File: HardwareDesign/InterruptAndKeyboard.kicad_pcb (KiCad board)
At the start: 2 copper layers, 150 x 90 mm, 39 parts, among them J001 Conn_02x40_Odd_Even, J501 Conn_01x20, J503 Conn_01x02, U401 74HCT74, U402 74HCT11, U403 74HCT147, U404 74HCT540, U405 74HCT574, U406 74HCT32, U407 74HCT32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

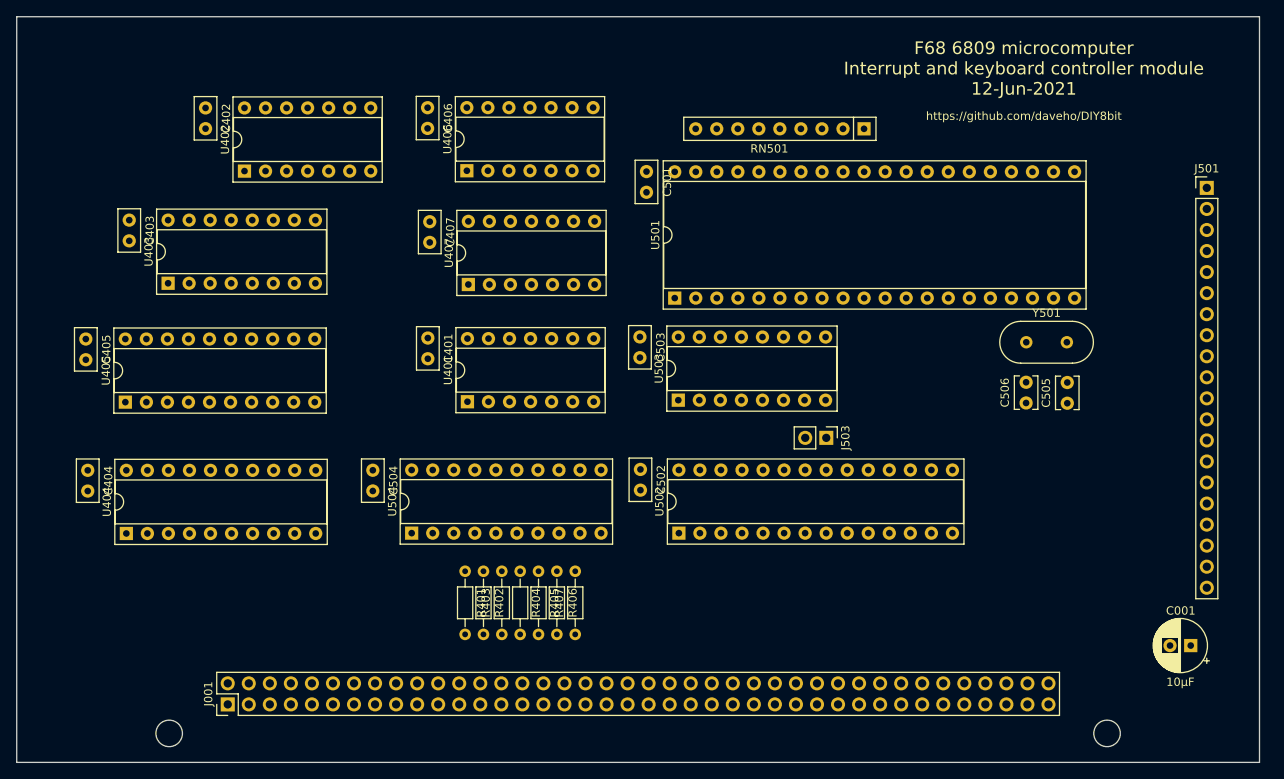
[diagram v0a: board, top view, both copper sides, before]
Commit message: tweak component placement
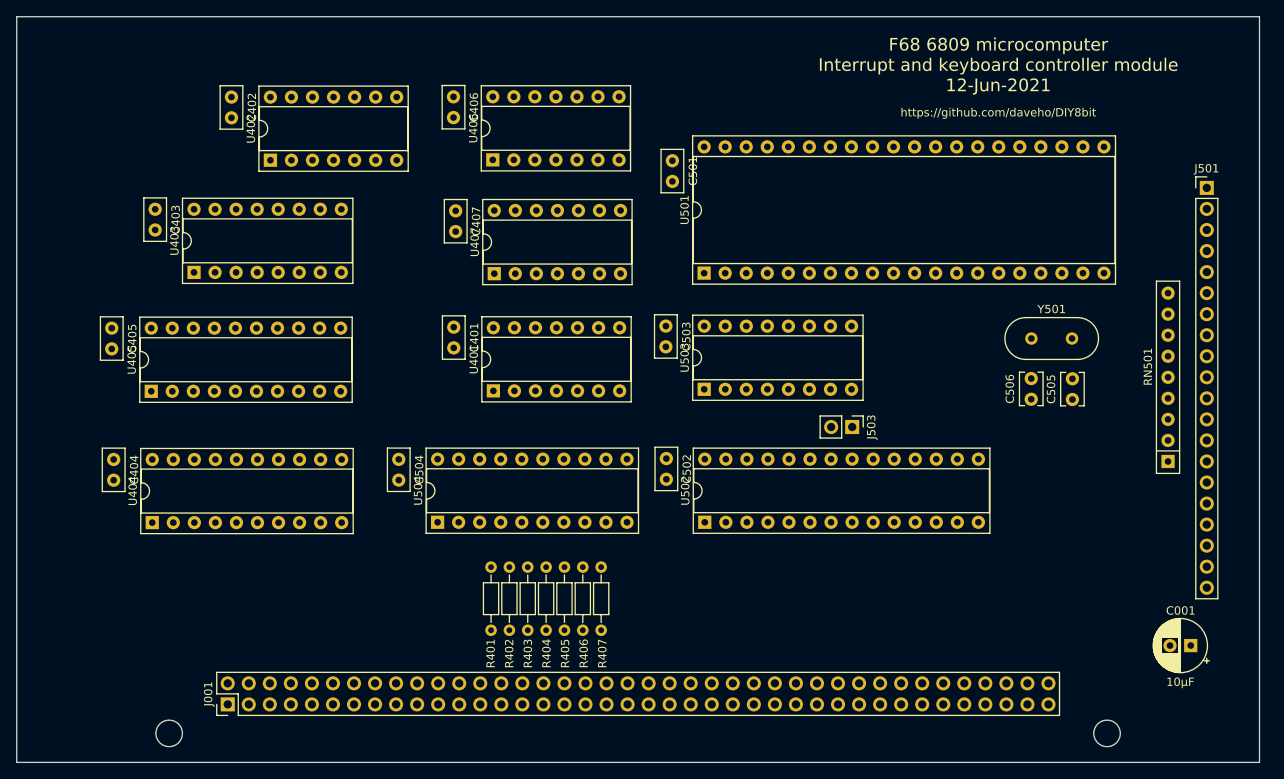
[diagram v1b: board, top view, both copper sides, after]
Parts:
- moved RN501 54.4 mm to (139.0, 53.7), turned to 90 degrees
- moved U501 4.65 mm to (83.0, 30.9)
- moved U503 3.39 mm to (83.0, 45.0)
- moved J503 3.39 mm to (100.8, 49.5)
- moved C401 3.39 mm to (52.8, 37.5)
- moved C504 3.39 mm to (46.1, 53.4)
- moved U401 3.39 mm to (57.5, 45.2)
- moved C402 3.39 mm to (25.9, 9.70)
- moved U402 3.39 mm to (30.6, 17.3)
- moved U406 3.39 mm to (57.5, 17.3)
- moved U407 3.39 mm to (57.6, 31.0)
- moved C403 3.39 mm to (16.7, 23.2)
- moved C404 3.39 mm to (11.7, 53.4)
- moved U403 3.39 mm to (21.4, 30.9)
- moved U405 3.39 mm to (16.2, 45.2)
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
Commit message: silkscreen tweaks
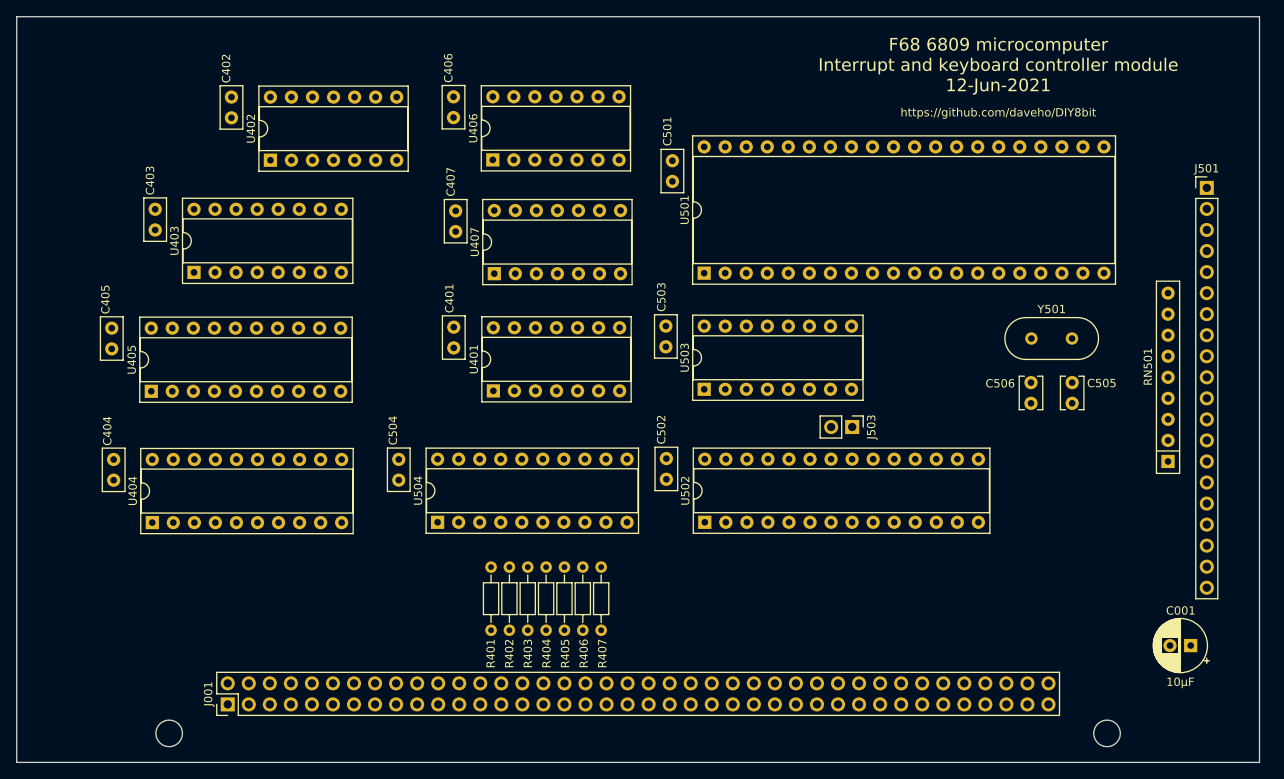
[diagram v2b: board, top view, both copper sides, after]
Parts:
- moved C506 0.49 mm to (122.4, 46.7)
- moved C505 0.46 mm to (127.4, 46.7)
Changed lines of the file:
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@@
     (descr "C, Disc series, Radial, pin pitch=2.50mm, , diameter*width=5*2.5mm^2, Capacitor, http://cdn-reichelt.de/documents/datenblatt/B300/DS_KERKO_TC.pdf")
     (tags "C Disc series Radial pin pitch 2.50mm  diameter 5mm width 2.5mm Capacitor")
-    (fp_text reference C401 (at 1.25 -2.5 90) (layer F.SilkS)
-      (effects (font (size 1 1) (thickness 0.15)))
-    )
-    (fp_text value "0.1 μF" (at 1.25 2.5 90) (layer F.Fab)
+    (fp_text reference C401 (at -3.48 0.5 90) (layer F.SilkS)
+      (effects (font (size 1 1) (thickness 0.15)))
+    )
+    (fp_text value "0.1 μF" (at -4.09 -0.8 90) (layer F.Fab)
       (effects (font (size 1 1) (thickness 0.15)))
     )
@@
     (descr "C, Disc series, Radial, pin pitch=2.50mm, , diameter*width=5*2.5mm^2, Capacitor, http://cdn-reichelt.de/documents/datenblatt/B300/DS_KERKO_TC.pdf")
     (tags "C Disc series Radial pin pitch 2.50mm  diameter 5mm width 2.5mm Capacitor")
-    (fp_text reference C402 (at 1.25 -2.5 90) (layer F.SilkS)
-      (effects (font (size 1 1) (thickness 0.15)))
-    )
-    (fp_text value "0.1 μF" (at 1.25 2.5 90) (layer F.Fab)
+    (fp_text reference C402 (at -3.46 0.62 90) (layer F.SilkS)
+      (effects (font (size 1 1) (thickness 0.15)))
+    )
+    (fp_text value "0.1 μF" (at -4.06 -0.65 90) (layer F.Fab)
       (effects (font (size 1 1) (thickness 0.15)))
     )
@@
     (descr "C, Disc series, Radial, pin pitch=2.50mm, , diameter*width=5*2.5mm^2, Capacitor, http://cdn-reichelt.de/documents/datenblatt/B300/DS_KERKO_TC.pdf")
     (tags "C Disc series Radial pin pitch 2.50mm  diameter 5mm width 2.5mm Capacitor")
-    (fp_text reference C403 (at 1.25 -2.5 90) (layer F.SilkS)
-      (effects (font (size 1 1) (thickness 0.15)))
-    )
-    (fp_text value "0.1 μF" (at 1.25 2.5 90) (layer F.Fab)
+    (fp_text reference C403 (at -3.48 0.59 90) (layer F.SilkS)
+      (effects (font (size 1 1) (thickness 0.15)))
+    )
+    (fp_text value "0.1 μF" (at -4.1 -0.66 90) (layer F.Fab)
       (effects (font (size 1 1) (thickness 0.15)))
     )
@@
     (descr "C, Disc series, Radial, pin pitch=2.50mm, , diameter*width=5*2.5mm^2, Capacitor, http://cdn-reichelt.de/documents/datenblatt/B300/DS_KERKO_TC.pdf")
     (tags "C Disc series Radial pin pitch 2.50mm  diameter 5mm width 2.5mm Capacitor")
-    (fp_text reference C404 (at 1.25 -2.5 90) (layer F.SilkS)
-      (effects (font (size 1 1) (thickness 0.15)))
-    )
-    (fp_text value "0.1 μF" (at 1.25 2.5 90) (layer F.Fab)
+    (fp_text reference C404 (at -3.44 0.74 90) (layer F.SilkS)
+      (effects (font (size 1 1) (thickness 0.15)))
+    )
+    (fp_text value "0.1 μF" (at -4.04 -0.54 90) (layer F.Fab)
       (effects (font (size 1 1) (thickness 0.15)))
     )
@@
     (descr "C, Disc series, Radial, pin pitch=2.50mm, , diameter*width=5*2.5mm^2, Capacitor, http://cdn-reichelt.de/documents/datenblatt/B300/DS_KERKO_TC.pdf")
     (tags "C Disc series Radial pin pitch 2.50mm  diameter 5mm width 2.5mm Capacitor")
-    (fp_text reference C405 (at 1.25 -2.5 90) (layer F.SilkS)
-      (effects (font (size 1 1) (thickness 0.15)))
-    )
-    (fp_text value "0.1 μF" (at 1.25 2.5 90) (layer F.Fab)
+    (fp_text reference C405 (at -3.47 0.74 90) (layer F.SilkS)
+      (effects (font (size 1 1) (thickness 0.15)))
+    )
+    (fp_text value "0.1 μF" (at -4.06 -0.62 90) (layer F.Fab)
       (effects (font (size 1 1) (thickness 0.15)))
     )
@@
     (descr "C, Disc series, Radial, pin pitch=2.50mm, , diameter*width=5*2.5mm^2, Capacitor, http://cdn-reichelt.de/documents/datenblatt/B300/DS_KERKO_TC.pdf")
     (tags "C Disc series Radial pin pitch 2.50mm  diameter 5mm width 2.5mm Capacitor")
-    (fp_text reference C406 (at 1.25 -2.5 90) (layer F.SilkS)
-      (effects (font (size 1 1) (thickness 0.15)))
-    )
-    (fp_text value "0.1 μF" (at 1.25 2.5 90) (layer F.Fab)
+    (fp_text reference C406 (at -3.48 0.6 90) (layer F.SilkS)
+      (effects (font (size 1 1) (thickness 0.15)))
+    )
+    (fp_text value "0.1 μF" (at -4.07 -0.72 90) (layer F.Fab)
       (effects (font (size 1 1) (thickness 0.15)))
     )
@@
     (descr "C, Disc series, Radial, pin pitch=2.50mm, , diameter*width=5*2.5mm^2, Capacitor, http://cdn-reichelt.de/documents/datenblatt/B300/DS_KERKO_TC.pdf")
     (tags "C Disc series Radial pin pitch 2.50mm  diameter 5mm width 2.5mm Capacitor")
-    (fp_text reference C407 (at 1.25 -2.5 90) (layer F.SilkS)
-      (effects (font (size 1 1) (thickness 0.15)))
-    )
-    (fp_text value "0.1 μF" (at 1.25 2.5 90) (layer F.Fab)
+    (fp_text reference C407 (at -3.51 0.58 90) (layer F.SilkS)
+      (effects (font (size 1 1) (thickness 0.15)))
+    )
+    (fp_text value "0.1 μF" (at -4.05 -0.62 90) (layer F.Fab)
       (effects (font (size 1 1) (thickness 0.15)))
     )
@@
     (descr "C, Disc series, Radial, pin pitch=2.50mm, , diameter*width=5*2.5mm^2, Capacitor, http://cdn-reichelt.de/documents/datenblatt/B300/DS_KERKO_TC.pdf")
     (tags "C Disc series Radial pin pitch 2.50mm  diameter 5mm width 2.5mm Capacitor")
-    (fp_text reference C501 (at 1.25 -2.5 90) (layer F.SilkS)
-      (effects (font (size 1 1) (thickness 0.15)))
-    )
-    (fp_text value "0.1 μF" (at 1.25 2.5 90) (layer F.Fab)
+    (fp_text reference C501 (at -3.55 0.59 90) (layer F.SilkS)
+      (effects (font (size 1 1) (thickness 0.15)))
+    )
+    (fp_text value "0.1 μF" (at -4.15 -0.73 90) (layer F.Fab)
       (effects (font (size 1 1) (thickness 0.15)))
     )
@@
     (descr "C, Disc series, Radial, pin pitch=2.50mm, , diameter*width=5*2.5mm^2, Capacitor, http://cdn-reichelt.de/documents/datenblatt/B300/DS_KERKO_TC.pdf")
     (tags "C Disc series Radial pin pitch 2.50mm  diameter 5mm width 2.5mm Capacitor")
-    (fp_text reference C502 (at 1.25 -2.5 90) (layer F.SilkS)
-      (effects (font (size 1 1) (thickness 0.15)))
-    )
-    (fp_text value "0.1 μF" (at 1.25 2.5 90) (layer F.Fab)
+    (fp_text reference C502 (at -3.5 0.59 90) (layer F.SilkS)
+      (effects (font (size 1 1) (thickness 0.15)))
+    )
+    (fp_text value "0.1 μF" (at -4.11 -0.68 90) (layer F.Fab)
       (effects (font (size 1 1) (thickness 0.15)))
     )
@@
     (descr "C, Disc series, Radial, pin pitch=2.50mm, , diameter*width=5*2.5mm^2, Capacitor, http://cdn-reichelt.de/documents/datenblatt/B300/DS_KERKO_TC.pdf")
     (tags "C Disc series Radial pin pitch 2.50mm  diameter 5mm width 2.5mm Capacitor")
-    (fp_text reference C503 (at 1.25 -2.5 90) (layer F.SilkS)
-      (effects (font (size 1 1) (thickness 0.15)))
-    )
-    (fp_text value "0.1 μF" (at 1.25 2.5 90) (layer F.Fab)
+    (fp_text reference C503 (at -3.51 0.52 90) (layer F.SilkS)
+      (effects (font (size 1 1) (thickness 0.15)))
+    )
+    (fp_text value "0.1 μF" (at -4.13 -0.83 90) (layer F.Fab)
       (effects (font (size 1 1) (thickness 0.15)))
     )
@@
     (descr "C, Disc series, Radial, pin pitch=2.50mm, , diameter*width=5*2.5mm^2, Capacitor, http://cdn-reichelt.de/documents/datenblatt/B300/DS_KERKO_TC.pdf")
     (tags "C Disc series Radial pin pitch 2.50mm  diameter 5mm width 2.5mm Capacitor")
-    (fp_text reference C504 (at 1.25 -2.5 90) (layer F.SilkS)
-      (effects (font (size 1 1) (thickness 0.15)))
-    )
-    (fp_text value "0.1 μF" (at 1.25 2.5 90) (layer F.Fab)
+    (fp_text reference C504 (at -3.49 0.68 90) (layer F.SilkS)
+      (effects (font (size 1 1) (thickness 0.15)))
+    )
+    (fp_text value "0.1 μF" (at -4.08 -0.61 90) (layer F.Fab)
       (effects (font (size 1 1) (thickness 0.15)))
     )
@@
   )
   (module Capacitor_THT:C_Disc_D3.8mm_W2.6mm_P2.50mm (layer Front)
-    (at 127.42 46.2 90)
+    (at 127.39 46.66 90)
     (descr "C, Disc series, Radial, pin pitch=2.50mm, , diameter*width=3.8*2.6mm^2, Capacitor, http://www.vishay.com/docs/45233/krseries.pdf")
     (tags "C Disc series Radial pin pitch 2.50mm  diameter 3.8mm width 2.6mm Capacitor")
-    (fp_text reference C505 (at 1.25 -2.55 90) (layer F.SilkS)
-      (effects (font (size 1 1) (thickness 0.15)))
-    )
-    (fp_text value 30pF (at 1.25 2.55 90) (layer F.Fab)
+    (fp_text reference C505 (at 2.41 3.58 180) (layer F.SilkS)
+      (effects (font (size 1 1) (thickness 0.15)))
+    )
+    (fp_text value 30pF (at 0.69 3.61 180) (layer F.Fab)
       (effects (font (size 1 1) (thickness 0.15)))
     )
@@
   )
   (module Capacitor_THT:C_Disc_D3.8mm_W2.6mm_P2.50mm (layer Front)
-    (at 122.45 46.17 90)
+    (at 122.42 46.66 90)
     (descr "C, Disc series, Radial, pin pitch=2.50mm, , diameter*width=3.8*2.6mm^2, Capacitor, http://www.vishay.com/docs/45233/krseries.pdf")
     (tags "C Disc series Radial pin pitch 2.50mm  diameter 3.8mm width 2.6mm Capacitor")
-    (fp_text reference C506 (at 1.25 -2.55 90) (layer F.SilkS)
-      (effects (font (size 1 1) (thickness 0.15)))
-    )
-    (fp_text value 30pF (at 1.25 2.55 90) (layer F.Fab)
-      (effects (font (size 1 1) (thickness 0.15)))
-    )
+    (fp_text reference C506 (at 2.38 -3.71 180) (layer F.SilkS)
+      (effects (font (size 1 1) (thickness 0.15)))
+    )
+    (fp_text value 30pF (at 0.66 -3.54 180) (layer F.Fab)
+      (effects (font (size 1 1) (thickness 0.15)))
+    )

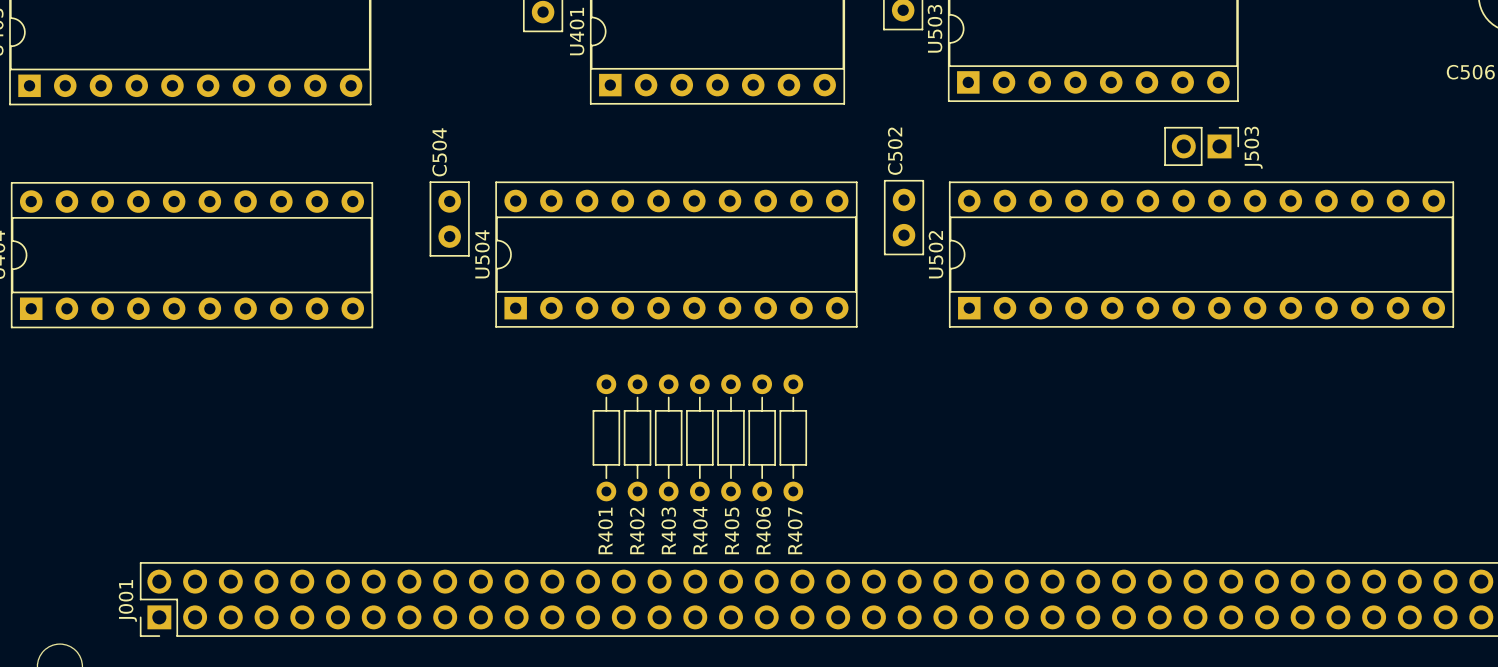
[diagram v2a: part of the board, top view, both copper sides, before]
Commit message: working on routing data bus connections
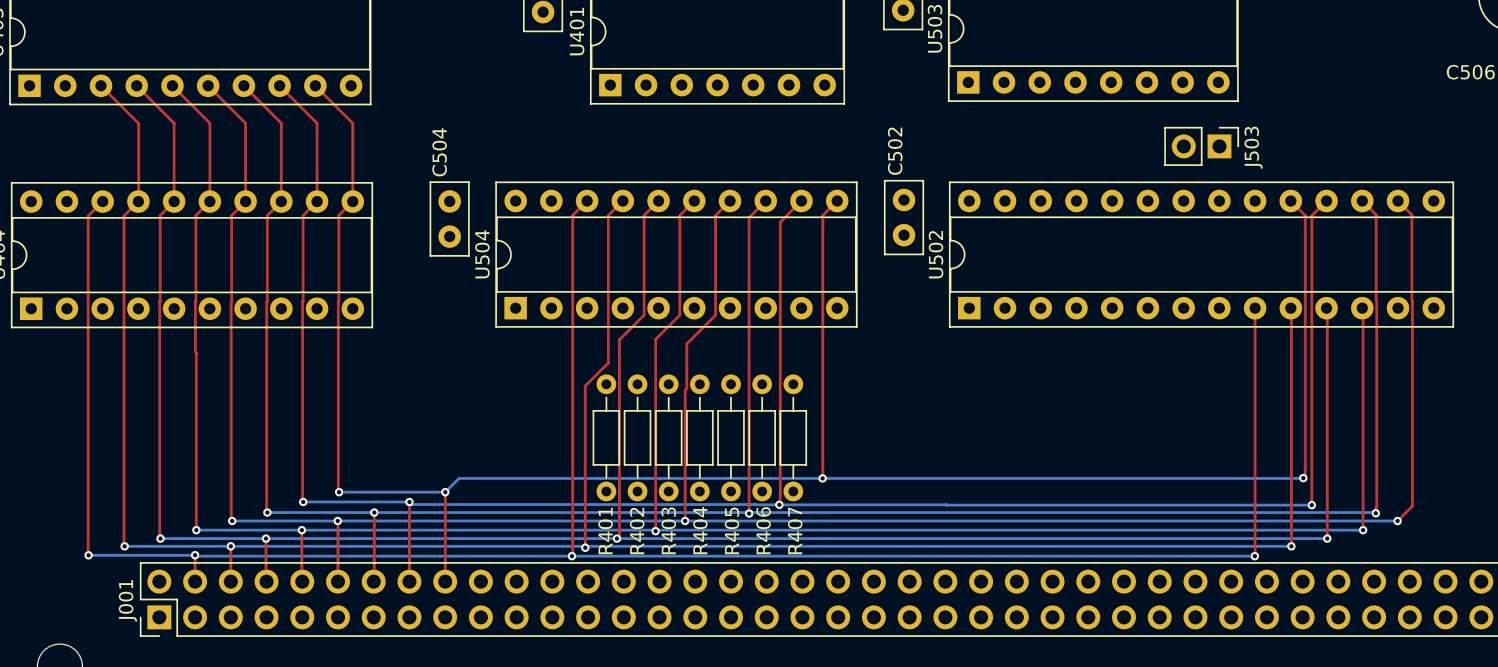
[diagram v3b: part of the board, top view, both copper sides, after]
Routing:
- net /D4: track 0.00 -> 167.5 mm, vias 0 -> 4
- net /D1: track 0.00 -> 162.5 mm, vias 0 -> 4
- net /D2: track 0.00 -> 161.4 mm, vias 0 -> 4
- net /D5: track 0.00 -> 161.1 mm, vias 0 -> 4
- net /D3: track 0.00 -> 160.2 mm, vias 0 -> 4
- net /D0: track 0.00 -> 153.7 mm, vias 0 -> 4
- net /D6: track 0.00 -> 152.9 mm, vias 0 -> 4
- net /D7: track 0.00 -> 146.1 mm, vias 0 -> 4
